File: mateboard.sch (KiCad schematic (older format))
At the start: 16 parts

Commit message: wip gpio
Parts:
- removed C?: 10uF/10V, symbol C
- removed R?: 10k, symbol R
- removed U?: 24LC32AT-I, TO_SOT_Packages_SMD:SOT-23-5, symbol AT24CS32-STUM
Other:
- moved on the sheet: R?
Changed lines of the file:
@@
 $EndSheet
 $Sheet
-S 6900 850  1250 1650
+S 6900 850  1250 2100
 U 58ABDF44
 F0 "MMC Interface" 60
@@
 	8475 1200 8475 2100
 Wire Wire Line
-	8475 2100 8475 2850
+	8475 2100 8475 3250
 Wire Wire Line
 	9225 2200 9150 2200
@@
 	8475 2100 9225 2100
 Wire Wire Line
-	8475 2850 8150 2850
+	8475 3250 8150 3250
 $Comp
 L USB_DC #PWR?
@@
 $EndComp
 Wire Wire Line
-	3850 2800 6350 2800
+	3850 2800 6500 2800
 Text Label 4400 2800 2    60   ~ 0
 USB1_OCn
 Wire Wire Line
-	6350 2400 6900 2400
+	6500 2400 6900 2400
 $Sheet
 S 4400 3000 1725 600
@@
 $EndSheet
 Wire Wire Line
-	6350 2800 6350 2400
+	6500 2800 6500 2400
 Wire Wire Line
 	4400 2000 3850 2000
@@
 L R R?
 U 1 1 58BA190C
-P 6650 2850
-F 0 "R?" V 6730 2850 50  0000 C CNN
-F 1 "0R" V 6650 2850 50  0000 C CNN
-F 2 "" V 6580 2850 50  0001 C CNN
-F 3 "" H 6650 2850 50  0001 C CNN
-	1    6650 2850
+P 6650 3250
+F 0 "R?" V 6730 3250 50  0000 C CNN
+F 1 "0R" V 6650 3250 50  0000 C CNN
+F 2 "" V 6580 3250 50  0001 C CNN
+F 3 "" H 6650 3250 50  0001 C CNN
+	1    6650 3250
 	0    1    1    0
 $EndComp
 Wire Wire Line
-	6800 2850 6900 2850
-Wire Wire Line
-	6500 2850 6300 2850
-Wire Wire Line
-	6300 2400 6300 2850
-Wire Wire Line
-	6300 2850 6300 3100
+	6800 3250 6900 3250
+Wire Wire Line
+	6300 2400 6300 3100
+Wire Wire Line
+	6300 3100 6300 3250
 Wire Wire Line
 	6300 2400 6125 2400
-Connection ~ 6300 2850
 Wire Wire Line
 	6125 1300 6400 1300
 Wire Wire Line
-	6400 1300 6400 3050
-Wire Wire Line
-	6400 3050 6900 3050
-Text Label 6425 3050 0    60   ~ 0
+	6400 1300 6400 3450
+Wire Wire Line
+	6400 3450 6900 3450
+Text Label 6425 3450 0    60   ~ 0
 GPIO0_7
 Wire Wire Line
@@
 Wire Wire Line
 	2000 1650 2600 1650
-$Comp
-L AT24CS32-STUM U?
-U 1 1 58BAF6FC
-P 1725 6725
-F 0 "U?" H 1525 6975 50  0000 C CNN
-F 1 "24LC32AT-I" H 2025 6425 50  0000 C CNN
-F 2 "TO_SOT_Packages_SMD:SOT-23-5" H 1725 6725 50  0001 C CIN
-F 3 "" H 1725 6725 50  0001 C CNN
-	1    1725 6725
-	1    0    0    -1
-$EndComp
-$Comp
-L VDD_3V3B #PWR?
-U 1 1 58BAF78B
-P 1725 6275
-F 0 "#PWR?" H 1725 6125 50  0001 C CNN
-F 1 "VDD_3V3B" H 1725 6425 50  0000 C CNN
-F 2 "" H 1725 6275 50  0000 C CNN
-F 3 "" H 1725 6275 50  0000 C CNN
-	1    1725 6275
-	1    0    0    -1
-$EndComp
-$Comp
-L C C?
-U 1 1 58BB10E1
-P 1025 6325
-F 0 "C?" V 1075 6400 50  0000 L CNN
-F 1 "10uF/10V" V 1150 6100 50  0000 L CNN
-F 2 "" H 1063 6175 50  0000 C CNN
-F 3 "" H 1025 6325 50  0000 C CNN
-	1    1025 6325
-	0    1    1    0
-$EndComp
-$Comp
-L GNDD #PWR?
-U 1 1 58BB10E8
-P 875 6325
-F 0 "#PWR?" H 875 6075 50  0001 C CNN
-F 1 "GNDD" V 875 6125 50  0000 C CNN
-F 2 "" H 875 6325 50  0000 C CNN
-F 3 "" H 875 6325 50  0000 C CNN
-	1    875  6325
-	0    1    1    0
-$EndComp
-Wire Wire Line
-	1175 6325 1225 6325
-Wire Wire Line
-	1225 6325 1725 6325
-Wire Wire Line
-	1725 6275 1725 6325
-Wire Wire Line
-	1725 6325 1725 6375
-Connection ~ 1725 6325
-$Comp
-L R R?
-U 1 1 58BB16F3
-P 1225 6725
-F 0 "R?" V 1305 6725 50  0000 C CNN
-F 1 "10k" V 1225 6725 50  0000 C CNN
-F 2 "" V 1155 6725 50  0001 C CNN
-F 3 "" H 1225 6725 50  0001 C CNN
-	1    1225 6725
-	1    0    0    -1
-$EndComp
-Wire Wire Line
-	1225 6875 1225 6925
-Wire Wire Line
-	1225 6925 1325 6925
-Wire Wire Line
-	1225 6325 1225 6575
-Connection ~ 1225 6325
-$Comp
-L GNDD #PWR?
-U 1 1 58BB231C
-P 1725 7125
-F 0 "#PWR?" H 1725 6875 50  0001 C CNN
-F 1 "GNDD" H 1725 6975 50  0000 C CNN
-F 2 "" H 1725 7125 50  0000 C CNN
-F 3 "" H 1725 7125 50  0000 C CNN
-	1    1725 7125
-	1    0    0    -1
-$EndComp
 Text Label 2000 1650 0    60   ~ 0
 I2C0_SDA
@@
 I2C0_SCL
 Wire Wire Line
-	2125 6775 2725 6775
-Wire Wire Line
-	2725 6625 2125 6625
-Text Label 2725 6625 2    60   ~ 0
+	6900 3650 6400 3650
+Wire Wire Line
+	6400 3750 6900 3750
+Text Label 6400 3750 0    60   ~ 0
 I2C0_SDA
-Text Label 2725 6775 2    60   ~ 0
-I2C0_SCL
-Text Label 2725 6625 2    60   ~ 0
-I2C0_SDA
-Text Label 2725 6775 2    60   ~ 0
-I2C0_SCL
-Wire Wire Line
-	6900 3250 6400 3250
-Wire Wire Line
-	6400 3350 6900 3350
-Text Label 6400 3350 0    60   ~ 0
-I2C0_SDA
-Text Label 6400 3250 0    60   ~ 0
+Text Label 6400 3650 0    60   ~ 0
 I2C0_SCL
 $Sheet
-S 6900 5150 1250 700
+S 6900 5550 1250 700
 U 58BD360A
 F0 "Boot Config" 60
 F1 "sysboot.sch" 60
-F2 "GPIO2_23" B R 8150 5350 60
-F3 "GPIO2_22" B R 8150 5250 60
-F4 "GPIO2_24" B R 8150 5450 60
-F5 "GPIO2_25" B R 8150 5550 60
+F2 "GPIO2_23" B R 8150 5750 60
+F3 "GPIO2_22" B R 8150 5650 60
+F4 "GPIO2_24" B R 8150 5850 60
+F5 "GPIO2_25" B R 8150 5950 60
 $EndSheet
 Wire Wire Line
 	6300 3100 6125 3100
 $Sheet
-S 6900 2750 1250 2150
+S 6900 3150 1250 2150
 U 589C7F89
 F0 "GPIO-I2C-SPI-UART" 60
 F1 "io.sch" 60
-F2 "MMC0_CD" I R 8150 2850 60
-F3 "GPIO3_20" B L 6900 2850 60
-F4 "GPIO0_7" B L 6900 3050 60
-F5 "I2C0_SCL" B L 6900 3250 60
-F6 "I2C0_SDA" B L 6900 3350 60
-F7 "I2C2_SCL" B R 8150 2950 60
-F8 "I2C2_SDA" B R 8150 3050 60
-F9 "I2C1_SCL" B R 8150 3150 60
-F10 "I2C1_SDA" B R 8150 3250 60
-F11 "AIN0" I R 8150 4200 60
-F12 "AIN1" I R 8150 4300 60
-F13 "AIN2" I R 8150 4400 60
-F14 "AIN3" I R 8150 4500 60
-F15 "AIN4" I R 8150 4600 60
-F16 "AIN5" I R 8150 4700 60
-F17 "AIN6" I R 8150 4800 60
-F18 "SPI1_SCLK" O R 8150 3350 60
-F19 "SPI1_CS0" O R 8150 3450 60
-F20 "SPI1_D0" O R 8150 3550 60
-F21 "GPIO3_21" B R 8150 3900 60
-F22 "GPIO3_19" B R 8150 4000 60
-F23 "SPI1_D1" O R 8150 3650 60
-F24 "UART2_RXD" I L 6900 3700 60
-F25 "UART2_TXD" O L 6900 3800 60
-F26 "UART1_RXD" I L 6900 3950 60
-F27 "UART1_TXD" O L 6900 4050 60
-F28 "UART0_RXD" I L 6900 4200 60
-F29 "UART0_TXD" O L 6900 4300 60
-$EndSheet
+F2 "MMC0_CD" I R 8150 3250 60
+F3 "GPIO3_20" B L 6900 3250 60
+F4 "GPIO0_7" B L 6900 3450 60
+F5 "I2C0_SCL" B L 6900 3650 60
+F6 "I2C0_SDA" B L 6900 3750 60
+F7 "I2C2_SCL" B R 8150 3350 60
+F8 "I2C2_SDA" B R 8150 3450 60
+F9 "I2C1_SCL" B R 8150 3550 60
+F10 "I2C1_SDA" B R 8150 3650 60
+F11 "AIN0" I R 8150 4600 60
+F12 "AIN1" I R 8150 4700 60
+F13 "AIN2" I R 8150 4800 60
+F14 "AIN3" I R 8150 4900 60
+F15 "AIN4" I R 8150 5000 60
+F16 "AIN5" I R 8150 5100 60
+F17 "AIN6" I R 8150 5200 60
+F18 "SPI1_SCLK" O R 8150 3750 60
+F19 "SPI1_CS0" O R 8150 3850 60
+F20 "SPI1_D0" O R 8150 3950 60
+F21 "GPIO3_21" B R 8150 4300 60
+F22 "GPIO3_19" B R 8150 4400 60
+F23 "SPI1_D1" O R 8150 4050 60
+F24 "UART2_RXD" I L 6900 4100 60
+F25 "UART2_TXD" O L 6900 4200 60
+F26 "UART1_RXD" I L 6900 4350 60
+F27 "UART1_TXD" O L 6900 4450 60
+F28 "UART0_RXD" I L 6900 4600 60
+F29 "UART0_TXD" O L 6900 4700 60
+$EndSheet
+Wire Wire Line
+	6300 3250 6500 3250
+Connection ~ 6300 3100
 $EndSCHEMATC

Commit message: gpio assignment done
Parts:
- added D? (x4): LTST-C191TBKT, symbol LED
- added Q? (x4): BSS138, TO_SOT_Packages_SMD:SOT-23, symbol BSS138
- added R? (x4): 1k, symbol R
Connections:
- net GNDD: now also Q?.2 (S), Q?.2 (S), Q?.2 (S), Q?.2 (S)
- net VDD_3V3B: now also R?.1, R?.1, R?.1, R?.1
- net MMC Interface/MMC0_CLK renamed MMC-GPIO/MMC0_CLK
- net MMC Interface/MMC0_CMD renamed MMC-GPIO/MMC0_CMD
- net MMC Interface/MMC0_DAT0 renamed MMC-GPIO/MMC0_DAT0
- net MMC Interface/MMC0_DAT1 renamed MMC-GPIO/MMC0_DAT1
- net MMC Interface/MMC0_DAT2 renamed MMC-GPIO/MMC0_DAT2
- net MMC Interface/MMC0_DAT3 renamed MMC-GPIO/MMC0_DAT3
- new net: D?.1 (K), Q?.3 (D) (x4)
- new net: D?.2 (A), R?.2 (x4)
- new net USR0: Q?.1 (G)
- new net USR1: Q?.1 (G)
- new net USR2: Q?.1 (G)
- new net USR3: Q?.1 (G)
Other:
- moved on the sheet: P?, R?

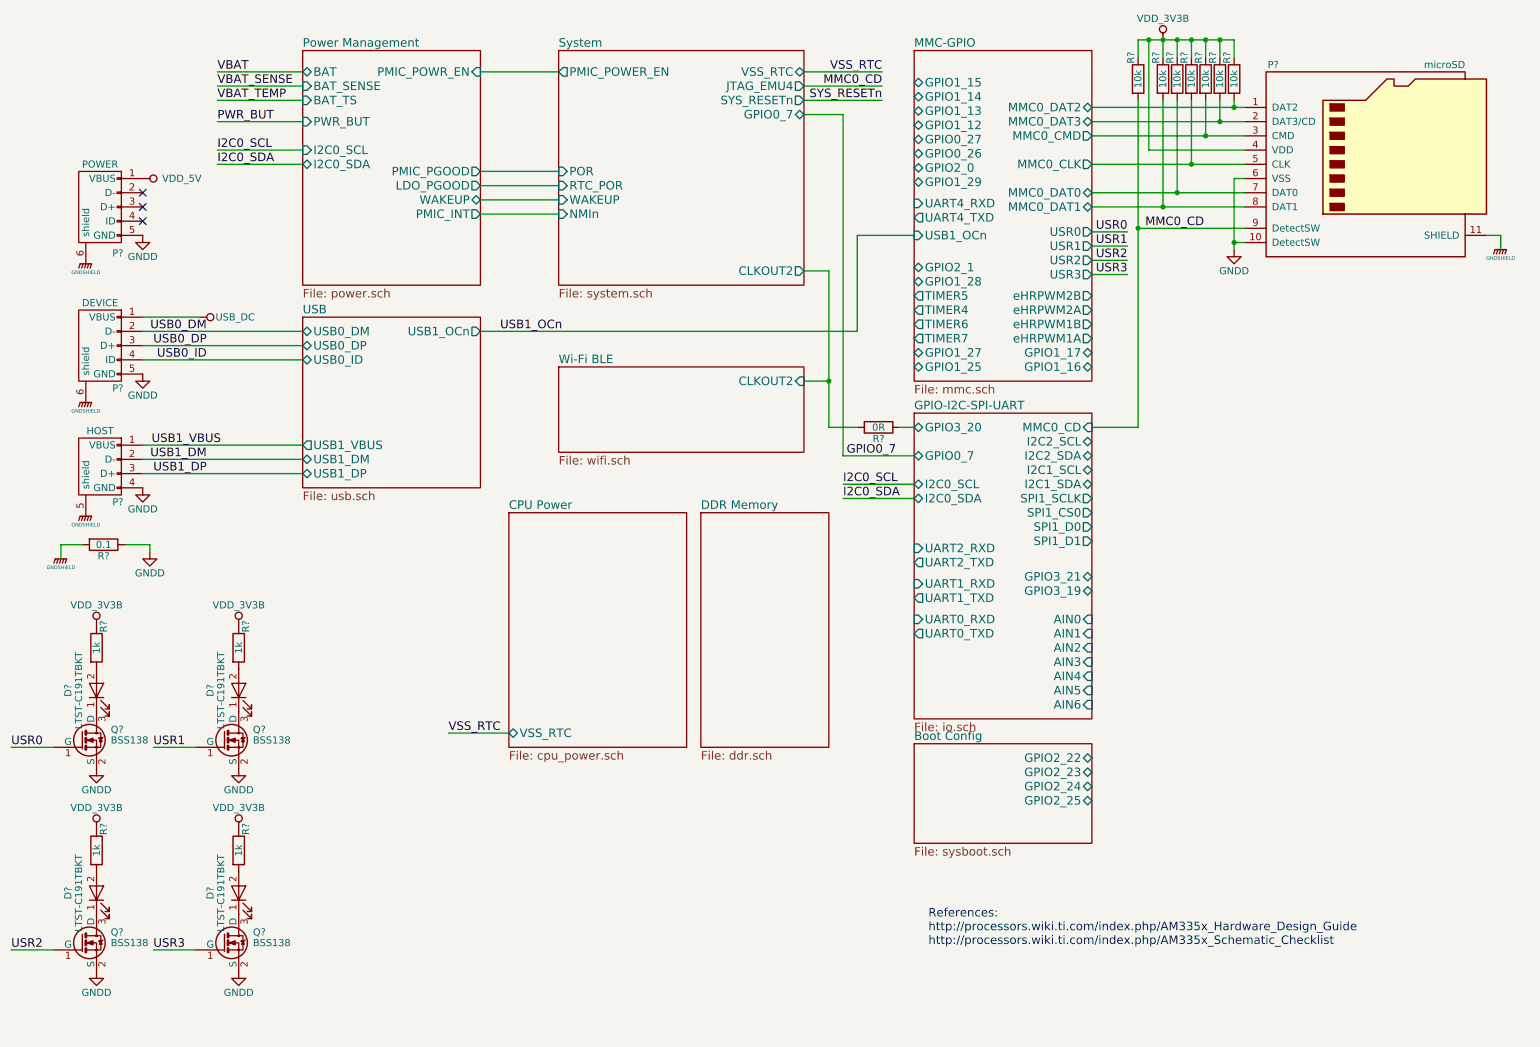
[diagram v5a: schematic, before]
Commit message: gpio connectors
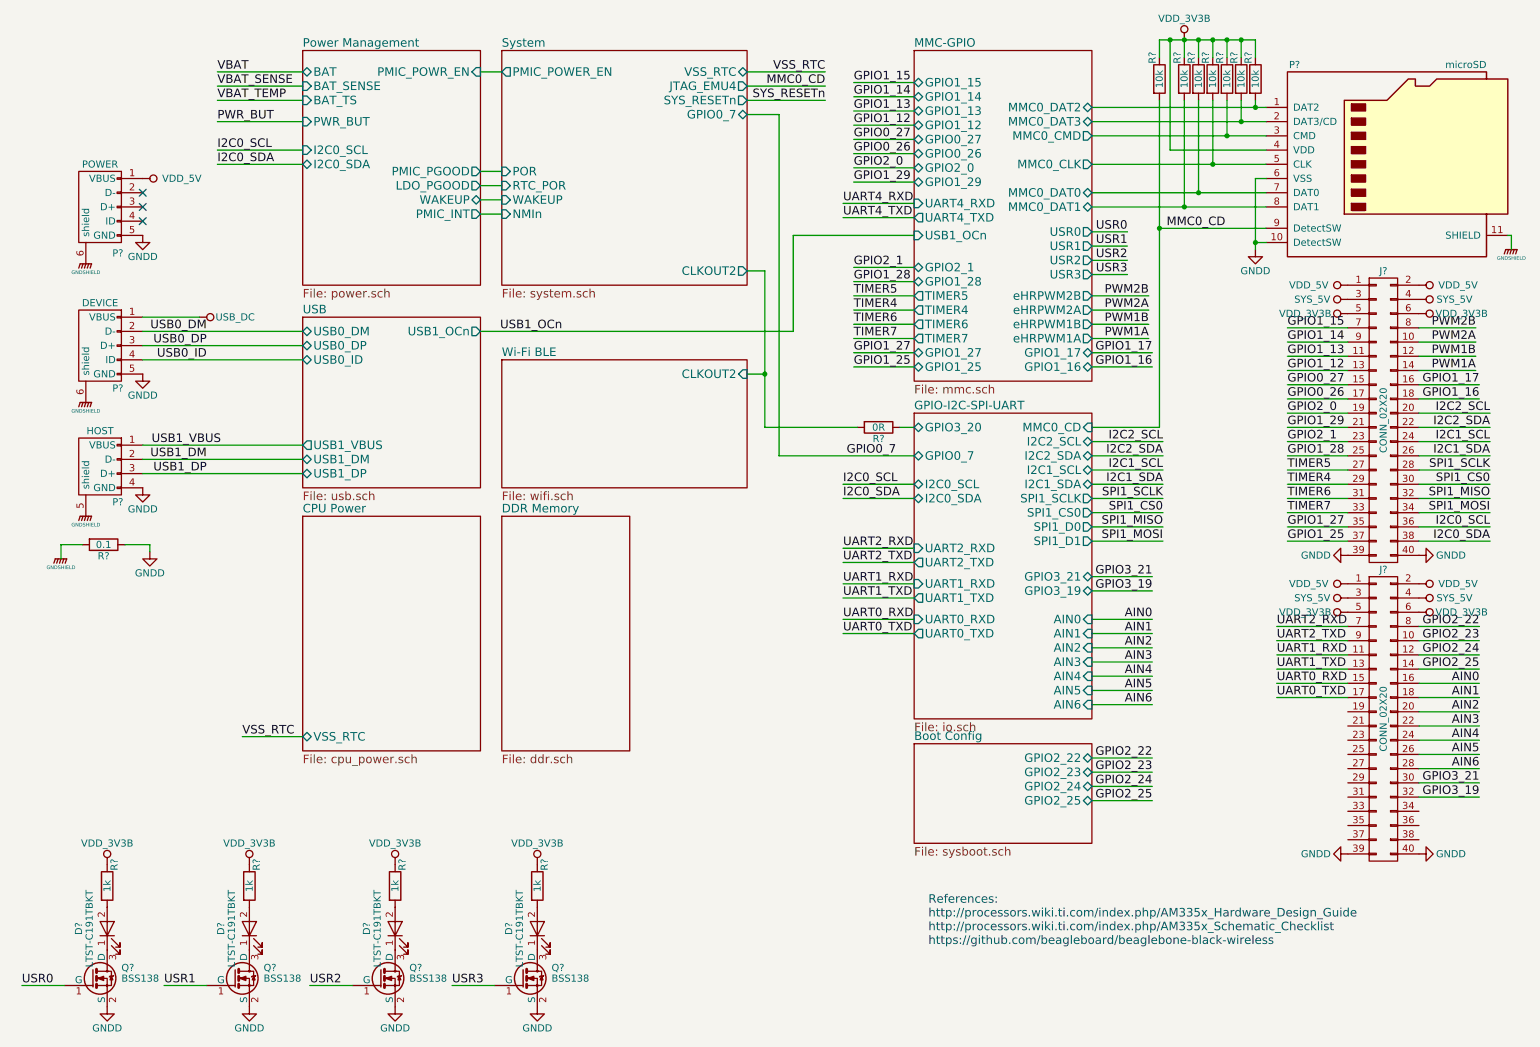
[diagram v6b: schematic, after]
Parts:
- added J? (x2): CONN_02X20, symbol CONN_02X20
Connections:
- net GNDD: now also J?.39 (P39), J?.39 (P39), J?.40 (P40), J?.40 (P40)
- net I2C0_SCL: now also J?.36 (P36)
- net I2C0_SDA: now also J?.38 (P38)
- net VDD_3V3B: now also J?.5 (P5), J?.5 (P5), J?.6 (P6), J?.6 (P6)
- net VDD_5V: now also J?.1 (P1), J?.1 (P1), J?.2 (P2), J?.2 (P2)
- new net AIN0: J?.16 (P16)
- new net AIN1: J?.18 (P18)
- new net AIN2: J?.20 (P20)
- new net AIN3: J?.22 (P22)
- new net AIN4: J?.24 (P24)
- new net AIN5: J?.26 (P26)
- new net AIN6: J?.28 (P28)
- new net GPIO0_26: J?.17 (P17)
- new net GPIO0_27: J?.15 (P15)
- new net GPIO1_12: J?.13 (P13)
- new net GPIO1_13: J?.11 (P11)
- new net GPIO1_14: J?.9 (P9)
- new net GPIO1_15: J?.7 (P7)
- new net GPIO1_16: J?.18 (P18)
- new net GPIO1_17: J?.16 (P16)
- new net GPIO1_25: J?.37 (P37)
- new net GPIO1_27: J?.35 (P35)
- new net GPIO1_28: J?.25 (P25)
- new net GPIO1_29: J?.21 (P21)
- new net GPIO2_0: J?.19 (P19)
- new net GPIO2_1: J?.23 (P23)
- new net GPIO2_22: J?.8 (P8)
- new net GPIO2_23: J?.10 (P10)
- new net GPIO2_24: J?.12 (P12)
- new net GPIO2_25: J?.14 (P14)
- new net GPIO3_19: J?.32 (P32)
- new net GPIO3_21: J?.30 (P30)
- new net I2C1_SCL: J?.24 (P24)
- new net I2C1_SDA: J?.26 (P26)
- new net I2C2_SCL: J?.20 (P20)
- new net I2C2_SDA: J?.22 (P22)
- new net PWM1A: J?.14 (P14)
- new net PWM1B: J?.12 (P12)
- new net PWM2A: J?.10 (P10)
- new net PWM2B: J?.8 (P8)
- new net SPI1_CS0: J?.30 (P30)
- new net SPI1_MISO: J?.32 (P32)
- new net SPI1_MOSI: J?.34 (P34)
- new net SPI1_SCLK: J?.28 (P28)
- new net SYS_5V: J?.3 (P3), J?.3 (P3), J?.4 (P4), J?.4 (P4)
- new net TIMER4: J?.29 (P29)
- new net TIMER5: J?.27 (P27)
- new net TIMER6: J?.31 (P31)
- new net TIMER7: J?.33 (P33)
- new net UART0_RXD: J?.15 (P15)
- new net UART0_TXD: J?.17 (P17)
- new net UART1_RXD: J?.11 (P11)
- new net UART1_TXD: J?.13 (P13)
- new net UART2_RXD: J?.7 (P7)
- new net UART2_TXD: J?.9 (P9)
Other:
- note added: "References:\nhttp://processors.wiki.ti.com/index.php/AM335x_Hardware_Design_Guide\nhttp://processors.wiki.ti.com/index.php/AM335x_Schematic_Checklist\nhttps://github.com/beagleboard/beaglebone-black-wireless"
- note removed: "References:\nhttp://processors.wiki.ti.com/index.php/AM335x_Hardware_Design_Guide\nhttp://processors.wiki.ti.com/index.php/AM335x_Schematic_Checklist\n"
- moved on the sheet: D?, P?, Q?, R?

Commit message: add doc and update sch
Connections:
- net GNDA: now reaches J?.37 (P37)
- net GNDA: now also J?.38 (P38)
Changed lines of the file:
@@
 Connection ~ 9100 700
 Wire Wire Line
-	8625 700  8700 700
-Wire Wire Line
-	8700 700  8800 700
-Wire Wire Line
-	8800 700  8900 700
-Wire Wire Line
-	8900 700  9000 700
-Wire Wire Line
-	9000 700  9100 700
-Wire Wire Line
-	9100 700  9200 700
-Wire Wire Line
-	9200 700  9300 700
+	8625 700  9300 700
 Wire Wire Line
 	9200 700  9200 825
@@
 	9300 1125 9300 1175
 Wire Wire Line
-	8150 1175 9300 1175
-Wire Wire Line
-	9300 1175 9375 1175
-Wire Wire Line
-	8150 1275 9200 1275
-Wire Wire Line
-	9200 1275 9375 1275
+	8150 1175 9375 1175
+Wire Wire Line
+	8150 1275 9375 1275
 Wire Wire Line
 	9200 1275 9200 1125
 Wire Wire Line
-	8150 1375 9100 1375
-Wire Wire Line
-	9100 1375 9375 1375
+	8150 1375 9375 1375
 Wire Wire Line
 	9100 1375 9100 1125
@@
 	8700 1475 8700 700
 Wire Wire Line
-	8150 1575 9000 1575
-Wire Wire Line
-	9000 1575 9375 1575
+	8150 1575 9375 1575
 Wire Wire Line
 	9000 1575 9000 1125
@@
 $EndComp
 Wire Wire Line
-	9300 1675 9300 2125
-Wire Wire Line
-	9300 2125 9300 2175
+	9300 1675 9300 2175
 Wire Wire Line
 	9300 1675 9375 1675
 Wire Wire Line
-	8150 1775 8900 1775
-Wire Wire Line
-	8900 1775 9375 1775
+	8150 1775 9375 1775
 Wire Wire Line
 	8900 1775 8900 1125
 Wire Wire Line
-	8150 1875 8800 1875
-Wire Wire Line
-	8800 1875 9375 1875
+	8150 1875 9375 1875
 Wire Wire Line
 	8800 1875 8800 1125
@@
 Connection ~ 8700 700
 Wire Wire Line
-	8625 1125 8625 2025
-Wire Wire Line
-	8625 2025 8625 3425
+	8625 1125 8625 3425
 Wire Wire Line
 	9375 2125 9300 2125
@@
 	6800 3425 6900 3425
 Wire Wire Line
-	5850 2325 5850 3050
-Wire Wire Line
-	5850 3050 5850 3425
+	5850 2325 5850 3425
 Wire Wire Line
 	5850 2325 5725 2325
@@
 Text Label 9450 5325 0    60   ~ 0
 UART0_TXD
+$Comp
+L GNDA #PWR?
+U 1 1 58C01623
+P 9950 6325
+F 0 "#PWR?" H 9950 6075 50  0001 C CNN
+F 1 "GNDA" V 9950 6125 50  0000 C CNN
+F 2 "" H 9950 6325 50  0000 C CNN
+F 3 "" H 9950 6325 50  0000 C CNN
+	1    9950 6325
+	0    1    1    0
+$EndComp
+$Comp
+L GNDA #PWR?
+U 1 1 58C0231F
+P 10450 6325
+F 0 "#PWR?" H 10450 6075 50  0001 C CNN
+F 1 "GNDA" V 10450 6125 50  0000 C CNN
+F 2 "" H 10450 6325 50  0000 C CNN
+F 3 "" H 10450 6325 50  0000 C CNN
+	1    10450 6325
+	0    -1   1    0
+$EndComp
 $EndSCHEMATC

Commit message: annotation, wip erc
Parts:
- gave numbers to parts that had none: 27
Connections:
- net PWR_BUT: now also J2.27 (P27)
- net USB1_DM: now also J2.33 (P33)
- net USB1_DP: now also J2.35 (P35)
- net USB1_VBUS: now also J2.31 (P31)
- net VBAT: now also J2.19 (P19), J2.21 (P21)
- net VBAT_SENSE: now also J2.23 (P23)
- net VBAT_TEMP: now also J2.25 (P25)
- no-connect marks 3 -> 4
